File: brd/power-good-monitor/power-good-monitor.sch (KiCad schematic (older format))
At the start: 23 parts, among them J1 POWER IN, J2 CASC IN, J3 POWER GOOD, J4 CASC OUT, Q1 DMP3028LK3-13, Q2 2N7002, Q3 DMP3028LK3-13, U1 TPS3701

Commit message: generado BoM
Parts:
- C1: Manufacturer (none) -> Yageo; Vendor (none) -> AC0805KKX7R0BB104
- C2: Manufacturer (none) -> Nichicon; Vendor (none) -> UWZ1C471MCL1GS
- D1: Manufacturer (none) -> Kingbright; Vendor (none) -> AP2012SRCPRV
- D2: Manufacturer (none) -> Micro Commercial Components; Vendor (none) -> MMSZ4699-TP
- D3: Manufacturer (none) -> Kingbright; Vendor (none) -> APT2012CGCK
- F1: Manufacturer (none) -> Bel Fuse; Vendor (none) -> 0679L7000-05
- J1: Manufacturer (none) -> Phoenix Contact; Vendor (none) -> 1888687
- J3: footprint Connectors_Molex:Molex_SPOX-5267_22-03-5025_02x2.54mm_Straight -> Connectors_Molex:Molex_KK-6410-02_02x2.54mm_Straight; Manufacturer (none) -> Molex; Vendor (none) -> 22-23-5021
- Q1, Q3: value DMP3028LK3-13 -> DMP3028; Manufacturer (none) -> Diodes Incorporated; Vendor (none) -> DMP3028LK3-13
- Q2: Manufacturer (none) -> Diodes Incorporated; Vendor (none) -> 2N7002-7-F
- R1: Manufacturer (none) -> Yageo; Vendor (none) -> RC0805FR-071M58L
- R2: Manufacturer (none) -> Yageo; Vendor (none) -> RC0805FR-0723K7L
- R3: Manufacturer (none) -> Yageo; Vendor (none) -> RC0805FR-07133KL
- R4, R8: Manufacturer (none) -> Yageo; Vendor (none) -> RC0805JR-0710KL
- R5, R9: Manufacturer (none) -> Yageo; Vendor (none) -> RC0805JR-07330RL
- R6, R7: Manufacturer (none) -> Yageo; Vendor (none) -> RC0805JR-07100KL
- U1: Manufacturer (none) -> Texas Instruments; Vendor (none) -> TPS3701DDCR
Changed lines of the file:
@@
 P 5975 3125
 F 0 "Q1" H 6175 3175 50  0000 L CNN
-F 1 "DMP3028LK3-13" H 6175 3075 50  0000 L CNN
+F 1 "DMP3028" H 6175 3075 50  0000 L CNN
 F 2 "TO_SOT_Packages_SMD:TO-252-2" H 6175 3225 50  0001 C CNN
 F 3 "" H 5975 3125 50  0001 C CNN
+F 4 "DMP3028LK3-13" H 5975 3125 60  0001 C CNN "Vendor"
+F 5 "Diodes Incorporated" H 5975 3125 60  0001 C CNN "Manufacturer"
 	1    5975 3125
 	0    -1   -1   0
@@
 P 6775 3125
 F 0 "Q3" H 6975 3175 50  0000 L CNN
-F 1 "DMP3028LK3-13" H 6975 3075 50  0000 L CNN
+F 1 "DMP3028" H 6975 3075 50  0000 L CNN
 F 2 "TO_SOT_Packages_SMD:TO-252-2" H 6975 3225 50  0001 C CNN
 F 3 "" H 6775 3125 50  0001 C CNN
+F 4 "DMP3028LK3-13" H 6775 3125 60  0001 C CNN "Vendor"
+F 5 "Diodes Incorporated" H 6775 3125 60  0001 C CNN "Manufacturer"
 	1    6775 3125
 	0    1    -1   0
@@
 F 2 "Resistors_SMD:R_0805_HandSoldering" V 6180 3225 50  0001 C CNN
 F 3 "" H 6250 3225 50  0001 C CNN
+F 4 "RC0805JR-07100KL" V 6250 3225 60  0001 C CNN "Vendor"
+F 5 "Yageo" V 6250 3225 60  0001 C CNN "Manufacturer"
 	1    6250 3225
 	1    0    0    -1
@@
 F 2 "Resistors_SMD:R_0805_HandSoldering" V 6305 3625 50  0001 C CNN
 F 3 "" H 6375 3625 50  0001 C CNN
+F 4 "RC0805JR-0710KL" V 6375 3625 60  0001 C CNN "Vendor"
+F 5 "Yageo" V 6375 3625 60  0001 C CNN "Manufacturer"
 	1    6375 3625
 	1    0    0    -1
@@
 F 2 "Diodes_SMD:D_SOD-123" H 6500 3225 50  0001 C CNN
 F 3 "" H 6500 3225 50  0001 C CNN
+F 4 "MMSZ4699-TP" H 6500 3225 60  0001 C CNN "Vendor"
+F 5 "Micro Commercial Components" H 6500 3225 60  0001 C CNN "Manufacturer"
 	1    6500 3225
 	0    1    1    0
@@
 F 2 "Terminal_Blocks:TerminalBlock_Pheonix_MKDS1.5-2pol" H 3200 3025 50  0001 C CNN
 F 3 "" H 3200 3025 50  0001 C CNN
+F 4 "1888687" H 3200 3025 60  0001 C CNN "Vendor"
+F 5 "Phoenix Contact" H 3200 3025 60  0001 C CNN "Manufacturer"
 	1    3200 3025
 	-1   0    0    -1
@@
 F 2 "Capacitors_SMD:CP_Elec_8x10" H 7088 3075 50  0001 C CNN
 F 3 "" H 7050 3225 50  0001 C CNN
+F 4 "UWZ1C471MCL1GS" H 7050 3225 60  0001 C CNN "Vendor"
+F 5 "Nichicon" H 7050 3225 60  0001 C CNN "Manufacturer"
 	1    7050 3225
 	1    0    0    -1
@@
 F 1 "TPS3701" H 4975 3975 50  0000 C CNN
 F 2 "TO_SOT_Packages_SMD:SOT-23-6_Handsoldering" H 4775 3675 50  0001 C CNN
-F 3 "DOCUMENTATION" H 4775 3675 50  0001 C CNN
+F 3 "" H 4775 3675 50  0001 C CNN
+F 4 "TPS3701DDCR" H 4775 3675 60  0001 C CNN "Vendor"
+F 5 "Texas Instruments" H 4775 3675 60  0001 C CNN "Manufacturer"
 	1    4775 3675
 	1    0    0    -1
@@
 F 2 "Resistors_SMD:R_0805_HandSoldering" V 4080 3275 50  0001 C CNN
 F 3 "" H 4150 3275 50  0001 C CNN
+F 4 "RC0805FR-071M58L" V 4150 3275 60  0001 C CNN "Vendor"
+F 5 "Yageo" V 4150 3275 60  0001 C CNN "Manufacturer"
 	1    4150 3275
 	1    0    0    -1
@@
 F 2 "Resistors_SMD:R_0805_HandSoldering" V 4080 3675 50  0001 C CNN
 F 3 "" H 4150 3675 50  0001 C CNN
+F 4 "RC0805FR-0723K7L" V 4150 3675 60  0001 C CNN "Vendor"
+F 5 "Yageo" V 4150 3675 60  0001 C CNN "Manufacturer"
 	1    4150 3675
 	1    0    0    -1
@@
 F 2 "Resistors_SMD:R_0805_HandSoldering" V 4080 4075 50  0001 C CNN
 F 3 "" H 4150 4075 50  0001 C CNN
+F 4 "RC0805FR-07133KL" V 4150 4075 60  0001 C CNN "Vendor"
+F 5 "Yageo" V 4150 4075 60  0001 C CNN "Manufacturer"
 	1    4150 4075
 	1    0    0    -1
@@
 F 2 "Capacitors_SMD:C_0805_HandSoldering" H 4513 4225 50  0001 C CNN
 F 3 "" H 4475 4375 50  0001 C CNN
+F 4 "AC0805KKX7R0BB104" H 4475 4375 60  0001 C CNN "Vendor"
+F 5 "Yageo" H 4475 4375 60  0001 C CNN "Manufacturer"
 	1    4475 4375
 	1    0    0    -1
@@
 F 2 "Resistors_SMD:R_0805_HandSoldering" V 5330 3275 50  0001 C CNN
 F 3 "" H 5400 3275 50  0001 C CNN
+F 4 "RC0805JR-0710KL" V 5400 3275 60  0001 C CNN "Vendor"
+F 5 "Yageo" V 5400 3275 60  0001 C CNN "Manufacturer"
 	1    5400 3275
 	1    0    0    -1
@@
 F 2 "Fuse_Holders_and_Fuses:Fuse_0679H" V 7205 3025 50  0001 C CNN
 F 3 "" H 7275 3025 50  0001 C CNN
+F 4 "0679L7000-05" V 7275 3025 60  0001 C CNN "Vendor"
+F 5 "Bel Fuse" V 7275 3025 60  0001 C CNN "Manufacturer"
 	1    7275 3025
 	0    1    1    0
@@
 F 2 "LEDs:LED_0805_HandSoldering" H 7475 3600 50  0001 C CNN
 F 3 "" H 7475 3600 50  0001 C CNN
+F 4 "APT2012CGCK" H 7475 3600 60  0001 C CNN "Vendor"
+F 5 "Kingbright" H 7475 3600 60  0001 C CNN "Manufacturer"
 	1    7475 3600
 	0    1    -1   0
@@
 F 2 "Resistors_SMD:R_0805_HandSoldering" V 7405 3225 50  0001 C CNN
 F 3 "" H 7475 3225 50  0001 C CNN
+F 4 "RC0805JR-07330RL" V 7475 3225 60  0001 C CNN "Vendor"
+F 5 "Yageo" V 7475 3225 60  0001 C CNN "Manufacturer"
 	1    7475 3225
 	1    0    0    -1
@@
 F 2 "LEDs:LED_0805_HandSoldering" H 5675 3225 50  0001 C CNN
 F 3 "" H 5675 3225 50  0001 C CNN
+F 4 "AP2012SRCPRV" H 5675 3225 60  0001 C CNN "Vendor"
+F 5 "Kingbright" H 5675 3225 60  0001 C CNN "Manufacturer"
 	1    5675 3225
 	0    1    -1   0
@@
 F 0 "J3" H 5650 4075 50  0000 C CNN
 F 1 "POWER GOOD" V 5750 3925 50  0000 C CNN
-F 2 "Connectors_Molex:Molex_SPOX-5267_22-03-5025_02x2.54mm_Straight" H 5650 3975 50  0001 C CNN
+F 2 "Connectors_Molex:Molex_KK-6410-02_02x2.54mm_Straight" H 5650 3975 50  0001 C CNN
 F 3 "" H 5650 3975 50  0001 C CNN
+F 4 "22-23-5021" H 5650 3975 60  0001 C CNN "Vendor"
+F 5 "Molex" H 5650 3975 60  0001 C CNN "Manufacturer"
 	1    5650 3975
 	1    0    0    -1
@@
 F 2 "TO_SOT_Packages_SMD:SOT-23_Handsoldering" H 6475 3975 50  0001 L CIN
 F 3 "" H 6275 4050 50  0001 L CNN
+F 4 "2N7002-7-F" H 6275 4050 60  0001 C CNN "Vendor"
+F 5 "Diodes Incorporated" H 6275 4050 60  0001 C CNN "Manufacturer"
 	1    6275 4050
 	1    0    0    -1
@@
 F 2 "Resistors_SMD:R_0805_HandSoldering" V 5955 4250 50  0001 C CNN
 F 3 "" H 6025 4250 50  0001 C CNN
+F 4 "RC0805JR-07100KL" V 6025 4250 60  0001 C CNN "Vendor"
+F 5 "Yageo" V 6025 4250 60  0001 C CNN "Manufacturer"
 	1    6025 4250
 	1    0    0    -1
@@
 F 2 "Resistors_SMD:R_0805_HandSoldering" V 5605 3575 50  0001 C CNN
 F 3 "" H 5675 3575 50  0001 C CNN
+F 4 "RC0805JR-07330RL" V 5675 3575 60  0001 C CNN "Vendor"
+F 5 "Yageo" V 5675 3575 60  0001 C CNN "Manufacturer"
 	1    5675 3575
 	1    0    0    -1

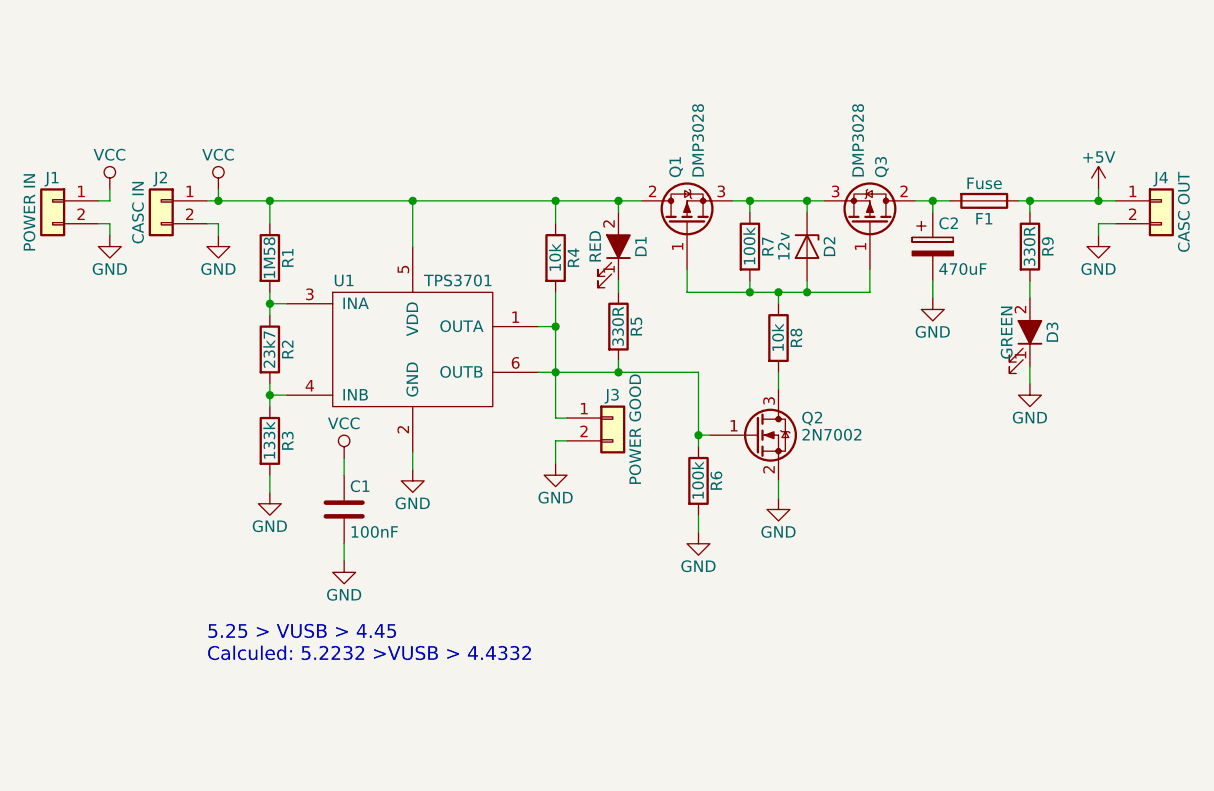
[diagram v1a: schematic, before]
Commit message: añadida salida de drenador abierto a pin de estado
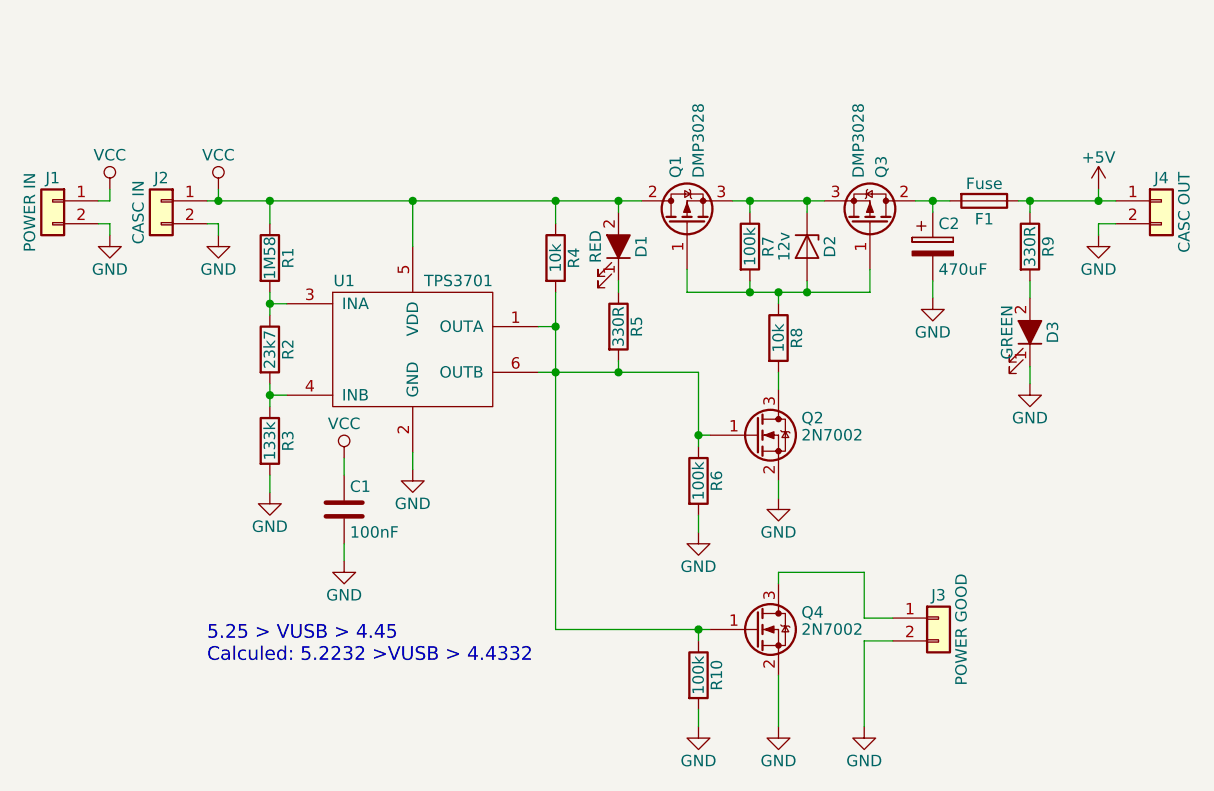
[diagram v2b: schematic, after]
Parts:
- added Q4: 2N7002, TO_SOT_Packages_SMD:SOT-23_Handsoldering, symbol 2N7002
- added R10: 100k, Resistors_SMD:R_0805_HandSoldering, symbol R
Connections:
- net GND: now also Q4.2 (S), R10.2
- net at Q2.1 (G), R4.2, R5.2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: now also Q4.1 (G), R10.1; no longer J3.1 (Pin_1)
- new net: J3.1 (Pin_1), Q4.3 (D)
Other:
- moved on the sheet: J3
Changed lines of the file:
@@
 $EndComp
 $Comp
-L GND #PWR01
+L GND #PWR4
 U 1 1 59FDB734
 P 3925 3175
-F 0 "#PWR01" H 3925 2925 50  0001 C CNN
+F 0 "#PWR4" H 3925 2925 50  0001 C CNN
 F 1 "GND" H 3925 3025 50  0000 C CNN
 F 2 "" H 3925 3175 50  0001 C CNN
@@
 $EndComp
 $Comp
-L +5V #PWR02
+L +5V #PWR16
 U 1 1 59FDB758
 P 7775 2975
-F 0 "#PWR02" H 7775 2825 50  0001 C CNN
+F 0 "#PWR16" H 7775 2825 50  0001 C CNN
 F 1 "+5V" H 7775 3115 50  0000 C CNN
 F 2 "" H 7775 2975 50  0001 C CNN
@@
 $EndComp
 $Comp
-L VCC #PWR03
+L VCC #PWR3
 U 1 1 59FDB77C
 P 3925 2975
-F 0 "#PWR03" H 3925 2825 50  0001 C CNN
+F 0 "#PWR3" H 3925 2825 50  0001 C CNN
 F 1 "VCC" H 3925 3125 50  0000 C CNN
 F 2 "" H 3925 2975 50  0001 C CNN
@@
 $EndComp
 $Comp
-L GND #PWR04
+L GND #PWR17
 U 1 1 59FDBA2F
 P 7775 3175
-F 0 "#PWR04" H 7775 2925 50  0001 C CNN
+F 0 "#PWR17" H 7775 2925 50  0001 C CNN
 F 1 "GND" H 7775 3025 50  0000 C CNN
 F 2 "" H 7775 3175 50  0001 C CNN
@@
 $EndComp
 $Comp
-L GND #PWR05
+L GND #PWR2
 U 1 1 59FDBD81
 P 3450 3175
-F 0 "#PWR05" H 3450 2925 50  0001 C CNN
+F 0 "#PWR2" H 3450 2925 50  0001 C CNN
 F 1 "GND" H 3450 3025 50  0000 C CNN
 F 2 "" H 3450 3175 50  0001 C CNN
@@
 $EndComp
 $Comp
-L VCC #PWR06
+L VCC #PWR1
 U 1 1 59FDBDA4
 P 3450 2975
-F 0 "#PWR06" H 3450 2825 50  0001 C CNN
+F 0 "#PWR1" H 3450 2825 50  0001 C CNN
 F 1 "VCC" H 3450 3125 50  0000 C CNN
 F 2 "" H 3450 2975 50  0001 C CNN
@@
 $EndComp
 $Comp
-L GND #PWR07
+L GND #PWR14
 U 1 1 59FDC06B
 P 7050 3450
-F 0 "#PWR07" H 7050 3200 50  0001 C CNN
+F 0 "#PWR14" H 7050 3200 50  0001 C CNN
 F 1 "GND" H 7050 3300 50  0000 C CNN
 F 2 "" H 7050 3450 50  0001 C CNN
@@
 $EndComp
 $Comp
-L GND #PWR08
+L GND #PWR7
 U 1 1 59FDCB6E
 P 4475 4600
-F 0 "#PWR08" H 4475 4350 50  0001 C CNN
+F 0 "#PWR7" H 4475 4350 50  0001 C CNN
 F 1 "GND" H 4475 4450 50  0000 C CNN
 F 2 "" H 4475 4600 50  0001 C CNN
@@
 $EndComp
 $Comp
-L VCC #PWR09
+L VCC #PWR6
 U 1 1 59FDCBA3
 P 4475 4150
-F 0 "#PWR09" H 4475 4000 50  0001 C CNN
+F 0 "#PWR6" H 4475 4000 50  0001 C CNN
 F 1 "VCC" H 4475 4300 50  0000 C CNN
 F 2 "" H 4475 4150 50  0001 C CNN
@@
 $EndComp
 $Comp
-L GND #PWR010
+L GND #PWR5
 U 1 1 59FDCEE2
 P 4150 4300
-F 0 "#PWR010" H 4150 4050 50  0001 C CNN
+F 0 "#PWR5" H 4150 4050 50  0001 C CNN
 F 1 "GND" H 4150 4150 50  0000 C CNN
 F 2 "" H 4150 4300 50  0001 C CNN
@@
 $EndComp
 $Comp
-L GND #PWR011
+L GND #PWR8
 U 1 1 59FDCF17
 P 4775 4200
-F 0 "#PWR011" H 4775 3950 50  0001 C CNN
+F 0 "#PWR8" H 4775 3950 50  0001 C CNN
 F 1 "GND" H 4775 4050 50  0000 C CNN
 F 2 "" H 4775 4200 50  0001 C CNN
@@
 $EndComp
 $Comp
-L GND #PWR012
+L GND #PWR15
 U 1 1 59FDF170
 P 7475 3825
-F 0 "#PWR012" H 7475 3575 50  0001 C CNN
+F 0 "#PWR15" H 7475 3575 50  0001 C CNN
 F 1 "GND" H 7475 3675 50  0000 C CNN
 F 2 "" H 7475 3825 50  0001 C CNN
@@
 L Conn_01x02 J3
 U 1 1 59FDFE98
-P 5650 3975
-F 0 "J3" H 5650 4075 50  0000 C CNN
-F 1 "POWER GOOD" V 5750 3925 50  0000 C CNN
-F 2 "Connectors_Molex:Molex_KK-6410-02_02x2.54mm_Straight" H 5650 3975 50  0001 C CNN
-F 3 "" H 5650 3975 50  0001 C CNN
-F 4 "22-23-5021" H 5650 3975 60  0001 C CNN "Vendor"
-F 5 "Molex" H 5650 3975 60  0001 C CNN "Manufacturer"
-	1    5650 3975
+P 7075 4850
+F 0 "J3" H 7075 4950 50  0000 C CNN
+F 1 "POWER GOOD" V 7175 4800 50  0000 C CNN
+F 2 "Connectors_Molex:Molex_KK-6410-02_02x2.54mm_Straight" H 7075 4850 50  0001 C CNN
+F 3 "" H 7075 4850 50  0001 C CNN
+F 4 "22-23-5021" H 7075 4850 60  0001 C CNN "Vendor"
+F 5 "Molex" H 7075 4850 60  0001 C CNN "Manufacturer"
+	1    7075 4850
 	1    0    0    -1
 $EndComp
@@
 $EndComp
 $Comp
-L GND #PWR013
+L GND #PWR11
 U 1 1 59FE05D1
 P 6375 4325
-F 0 "#PWR013" H 6375 4075 50  0001 C CNN
+F 0 "#PWR11" H 6375 4075 50  0001 C CNN
 F 1 "GND" H 6375 4175 50  0000 C CNN
 F 2 "" H 6375 4325 50  0001 C CNN
@@
 $EndComp
 $Comp
-L GND #PWR014
+L GND #PWR9
 U 1 1 59FE0694
 P 6025 4475
-F 0 "#PWR014" H 6025 4225 50  0001 C CNN
+F 0 "#PWR9" H 6025 4225 50  0001 C CNN
 F 1 "GND" H 6025 4325 50  0000 C CNN
 F 2 "" H 6025 4475 50  0001 C CNN
@@
 	6025 4050 6075 4050
 Wire Wire Line
-	5400 3425 5400 3975
+	5400 3425 5400 4900
 Wire Wire Line
 	5325 3775 6025 3775
 $Comp
-L GND #PWR015
+L GND #PWR13
 U 1 1 59FE2ED6
-P 5400 4175
-F 0 "#PWR015" H 5400 3925 50  0001 C CNN
-F 1 "GND" H 5400 4025 50  0000 C CNN
-F 2 "" H 5400 4175 50  0001 C CNN
-F 3 "" H 5400 4175 50  0001 C CNN
-	1    5400 4175
+P 6750 5325
+F 0 "#PWR13" H 6750 5075 50  0001 C CNN
+F 1 "GND" H 6750 5175 50  0000 C CNN
+F 2 "" H 6750 5325 50  0001 C CNN
+F 3 "" H 6750 5325 50  0001 C CNN
+	1    6750 5325
 	1    0    0    -1
 $EndComp
 Wire Wire Line
 	5675 3425 5675 3375
-Wire Wire Line
-	5400 4175 5400 4075
-Wire Wire Line
-	5400 4075 5450 4075
-Wire Wire Line
-	5400 3975 5450 3975
 Wire Wire Line
 	3875 3025 5775 3025
@@
 Connection ~ 6025 4050
 Connection ~ 5675 3775
+$Comp
+L 2N7002 Q4
+U 1 1 5A00337D
+P 6275 4900
+F 0 "Q4" H 6475 4975 50  0000 L CNN
+F 1 "2N7002" H 6475 4900 50  0000 L CNN
+F 2 "TO_SOT_Packages_SMD:SOT-23_Handsoldering" H 6475 4825 50  0001 L CIN
+F 3 "" H 6275 4900 50  0001 L CNN
+F 4 "2N7002-7-F" H 6275 4900 60  0001 C CNN "Vendor"
+F 5 "Diodes Incorporated" H 6275 4900 60  0001 C CNN "Manufacturer"
+	1    6275 4900
+	1    0    0    -1
+$EndComp
+$Comp
+L R R10
+U 1 1 5A00343D
+P 6025 5100
+F 0 "R10" V 6105 5100 50  0000 C CNN
+F 1 "100k" V 6025 5100 50  0000 C CNN
+F 2 "Resistors_SMD:R_0805_HandSoldering" V 5955 5100 50  0001 C CNN
+F 3 "" H 6025 5100 50  0001 C CNN
+F 4 "RC0805JR-07100KL" V 6025 5100 60  0001 C CNN "Vendor"
+F 5 "Yageo" V 6025 5100 60  0001 C CNN "Manufacturer"
+	1    6025 5100
+	1    0    0    -1
+$EndComp
+$Comp
+L GND #PWR10
+U 1 1 5A00352E
+P 6025 5325
+F 0 "#PWR10" H 6025 5075 50  0001 C CNN
+F 1 "GND" H 6025 5175 50  0000 C CNN
+F 2 "" H 6025 5325 50  0001 C CNN
+F 3 "" H 6025 5325 50  0001 C CNN
+	1    6025 5325
+	1    0    0    -1
+$EndComp
+$Comp
+L GND #PWR12
+U 1 1 5A003584
+P 6375 5325
+F 0 "#PWR12" H 6375 5075 50  0001 C CNN
+F 1 "GND" H 6375 5175 50  0000 C CNN
+F 2 "" H 6375 5325 50  0001 C CNN
+F 3 "" H 6375 5325 50  0001 C CNN
+	1    6375 5325
+	1    0    0    -1
+$EndComp
+Wire Wire Line
+	6750 5325 6750 4950
+Wire Wire Line
+	6750 4950 6875 4950
+Wire Wire Line
+	6375 5325 6375 5100
+Wire Wire Line
+	6025 5325 6025 5250
+Wire Wire Line
+	6025 4950 6025 4900
+Wire Wire Line
+	5400 4900 6075 4900
+Wire Wire Line
+	6375 4700 6375 4650
+Wire Wire Line
+	6375 4650 6750 4650
+Wire Wire Line
+	6750 4650 6750 4850
+Wire Wire Line
+	6750 4850 6875 4850
+Connection ~ 6025 4900
 $EndSCHEMATC
